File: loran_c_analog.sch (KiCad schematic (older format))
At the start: 54 parts, among them P601 DAC VCO, P602 DAC AGC, P603 LORAN In, P604 RSVD In, Q601 BD135, Q602 BD136, U601 TL072, U602 LD1117S33

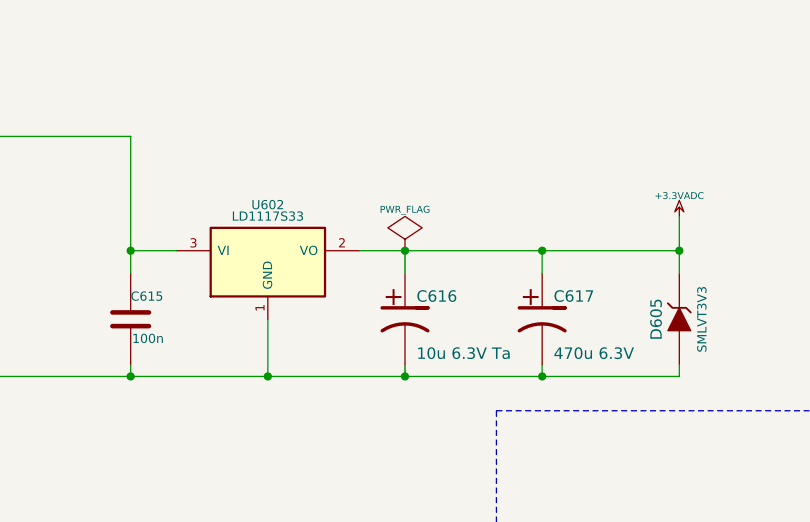
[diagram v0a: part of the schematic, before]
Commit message: FIXED: no more buses on hierarchical sheet ports
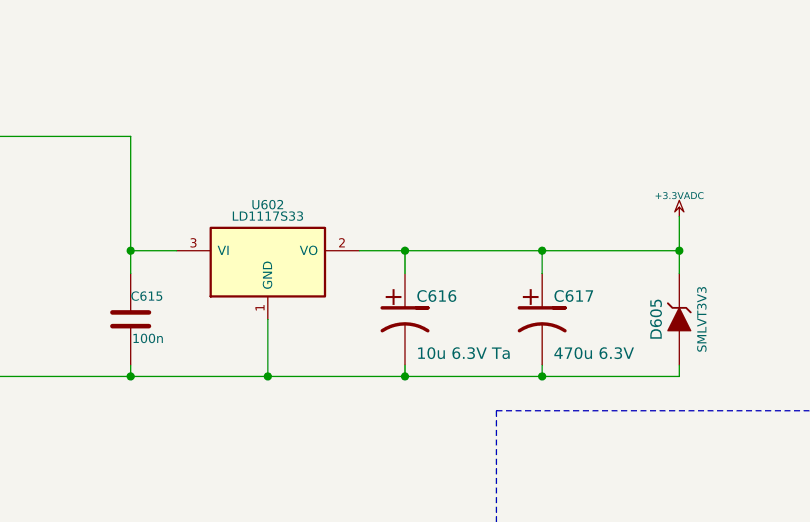
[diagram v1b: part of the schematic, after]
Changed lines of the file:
@@
 $Descr A4 11693 8268
 encoding utf-8
-Sheet 6 7
+Sheet 5 7
 Title "Analog part"
 Date ""
@@
 $EndComp
 $Comp
-L +3.3VADC #PWR088
+L +3.3VADC #PWR081
 U 1 1 52E38762
 P 7700 1650
-F 0 "#PWR088" H 7700 1770 20  0001 C CNN
+F 0 "#PWR081" H 7700 1770 20  0001 C CNN
 F 1 "+3.3VADC" H 7700 1740 30  0000 C CNN
 F 2 "" H 7700 1650 60  0000 C CNN
 F 3 "" H 7700 1650 60  0000 C CNN
 	1    7700 1650
-	1    0    0    -1
-$EndComp
-$Comp
-L PWR_FLAG #FLG089
-U 1 1 52E3A067
-P 6500 1800
-F 0 "#FLG089" H 6500 1895 30  0001 C CNN
-F 1 "PWR_FLAG" H 6500 1980 30  0000 C CNN
-F 2 "" H 6500 1800 60  0000 C CNN
-F 3 "" H 6500 1800 60  0000 C CNN
-	1    6500 1800
 	1    0    0    -1
 $EndComp
@@
 -7.5V
 $Comp
-L AGND #PWR090
+L AGND #PWR082
 U 1 1 52E3C710
 P 1150 2400
-F 0 "#PWR090" H 1150 2400 40  0001 C CNN
+F 0 "#PWR082" H 1150 2400 40  0001 C CNN
 F 1 "AGND" H 1150 2330 50  0000 C CNN
 F 2 "" H 1150 2400 60  0000 C CNN
@@
 $EndComp
 $Comp
-L AGND #PWR091
+L AGND #PWR083
 U 1 1 52E42BA3
 P 3600 4850
-F 0 "#PWR091" H 3600 4850 40  0001 C CNN
+F 0 "#PWR083" H 3600 4850 40  0001 C CNN
 F 1 "AGND" H 3600 4780 50  0000 C CNN
 F 2 "" H 3600 4850 60  0000 C CNN
@@
 $EndComp
 $Comp
-L AGND #PWR092
+L AGND #PWR084
 U 1 1 52E42BAE
 P 3900 4850
-F 0 "#PWR092" H 3900 4850 40  0001 C CNN
+F 0 "#PWR084" H 3900 4850 40  0001 C CNN
 F 1 "AGND" H 3900 4780 50  0000 C CNN
 F 2 "" H 3900 4850 60  0000 C CNN
@@
 $EndComp
 $Comp
-L AGND #PWR093
+L AGND #PWR085
 U 1 1 52E434DA
 P 3600 6550
-F 0 "#PWR093" H 3600 6550 40  0001 C CNN
+F 0 "#PWR085" H 3600 6550 40  0001 C CNN
 F 1 "AGND" H 3600 6480 50  0000 C CNN
 F 2 "" H 3600 6550 60  0000 C CNN
@@
 $EndComp
 $Comp
-L AGND #PWR094
+L AGND #PWR086
 U 1 1 52E434E0
 P 3900 6550
-F 0 "#PWR094" H 3900 6550 40  0001 C CNN
+F 0 "#PWR086" H 3900 6550 40  0001 C CNN
 F 1 "AGND" H 3900 6480 50  0000 C CNN
 F 2 "" H 3900 6550 60  0000 C CNN
@@
 $EndComp
 $Comp
-L PWR_FLAG #FLG095
+L PWR_FLAG #FLG087
 U 1 1 52E43900
 P 4600 1300
-F 0 "#FLG095" H 4600 1395 30  0001 C CNN
+F 0 "#FLG087" H 4600 1395 30  0001 C CNN
 F 1 "PWR_FLAG" H 4600 1480 30  0000 C CNN
 F 2 "" H 4600 1300 60  0000 C CNN
@@
 $EndComp
 $Comp
-L PWR_FLAG #FLG096
+L PWR_FLAG #FLG088
 U 1 1 52E4390B
 P 4600 3400
-F 0 "#FLG096" H 4600 3495 30  0001 C CNN
+F 0 "#FLG088" H 4600 3495 30  0001 C CNN
 F 1 "PWR_FLAG" H 4600 3580 30  0000 C CNN
 F 2 "" H 4600 3400 60  0000 C CNN
@@
 $EndComp
 $Comp
-L AGND #PWR097
+L AGND #PWR089
 U 1 1 52E4434F
 P 4600 5450
-F 0 "#PWR097" H 4600 5450 40  0001 C CNN
+F 0 "#PWR089" H 4600 5450 40  0001 C CNN
 F 1 "AGND" H 4600 5380 50  0000 C CNN
 F 2 "" H 4600 5450 60  0000 C CNN
@@
 $EndComp
 $Comp
-L AGND #PWR098
+L AGND #PWR090
 U 1 1 52E4435A
 P 4600 6550
-F 0 "#PWR098" H 4600 6550 40  0001 C CNN
+F 0 "#PWR090" H 4600 6550 40  0001 C CNN
 F 1 "AGND" H 4600 6480 50  0000 C CNN
 F 2 "" H 4600 6550 60  0000 C CNN
@@
 $EndComp
 $Comp
-L AGND #PWR099
+L AGND #PWR091
 U 1 1 52E476C2
 P 1600 5650
-F 0 "#PWR099" H 1600 5650 40  0001 C CNN
+F 0 "#PWR091" H 1600 5650 40  0001 C CNN
 F 1 "AGND" H 1600 5580 50  0000 C CNN
 F 2 "" H 1600 5650 60  0000 C CNN
@@
 $EndComp
 $Comp
-L AGND #PWR0100
+L AGND #PWR092
 U 1 1 52E4B7B5
 P 7950 4100
-F 0 "#PWR0100" H 7950 4100 40  0001 C CNN
+F 0 "#PWR092" H 7950 4100 40  0001 C CNN
 F 1 "AGND" H 7950 4030 50  0000 C CNN
 F 2 "" H 7950 4100 60  0000 C CNN
@@
 $EndComp
 $Comp
-L AGND #PWR0101
+L AGND #PWR093
 U 1 1 52E4C26B
 P 8450 4100
-F 0 "#PWR0101" H 8450 4100 40  0001 C CNN
+F 0 "#PWR093" H 8450 4100 40  0001 C CNN
 F 1 "AGND" H 8450 4030 50  0000 C CNN
 F 2 "" H 8450 4100 60  0000 C CNN
@@
 $EndComp
 $Comp
-L AGND #PWR0102
+L AGND #PWR094
 U 1 1 52E4D87E
 P 8200 4100
-F 0 "#PWR0102" H 8200 4100 40  0001 C CNN
+F 0 "#PWR094" H 8200 4100 40  0001 C CNN
 F 1 "AGND" H 8200 4030 50  0000 C CNN
 F 2 "" H 8200 4100 60  0000 C CNN
@@
 $EndComp
 $Comp
-L AGND #PWR0103
+L AGND #PWR095
 U 1 1 52E4EBFE
 P 9100 4100
-F 0 "#PWR0103" H 9100 4100 40  0001 C CNN
+F 0 "#PWR095" H 9100 4100 40  0001 C CNN
 F 1 "AGND" H 9100 4030 50  0000 C CNN
 F 2 "" H 9100 4100 60  0000 C CNN
@@
 $EndComp
 $Comp
-L AGND #PWR0104
+L AGND #PWR096
 U 1 1 52E4EC09
 P 9400 4100
-F 0 "#PWR0104" H 9400 4100 40  0001 C CNN
+F 0 "#PWR096" H 9400 4100 40  0001 C CNN
 F 1 "AGND" H 9400 4030 50  0000 C CNN
 F 2 "" H 9400 4100 60  0000 C CNN
@@
 $EndComp
 $Comp
-L +3.3VADC #PWR0105
+L +3.3VADC #PWR097
 U 1 1 52E4EC14
 P 9100 2750
-F 0 "#PWR0105" H 9100 2870 20  0001 C CNN
+F 0 "#PWR097" H 9100 2870 20  0001 C CNN
 F 1 "+3.3VADC" H 9100 2840 30  0000 C CNN
 F 2 "" H 9100 2750 60  0000 C CNN
@@
 $EndComp
 $Comp
-L AGND #PWR0106
+L AGND #PWR098
 U 1 1 52E53548
 P 10250 4100
-F 0 "#PWR0106" H 10250 4100 40  0001 C CNN
+F 0 "#PWR098" H 10250 4100 40  0001 C CNN
 F 1 "AGND" H 10250 4030 50  0000 C CNN
 F 2 "" H 10250 4100 60  0000 C CNN
@@
 $EndComp
 $Comp
-L AGND #PWR0107
+L AGND #PWR099
 U 1 1 52E545C4
 P 7950 5900
-F 0 "#PWR0107" H 7950 5900 40  0001 C CNN
+F 0 "#PWR099" H 7950 5900 40  0001 C CNN
 F 1 "AGND" H 7950 5830 50  0000 C CNN
 F 2 "" H 7950 5900 60  0000 C CNN
@@
 $EndComp
 $Comp
-L AGND #PWR0108
+L AGND #PWR0100
 U 1 1 52E545D0
 P 8450 5900
-F 0 "#PWR0108" H 8450 5900 40  0001 C CNN
+F 0 "#PWR0100" H 8450 5900 40  0001 C CNN
 F 1 "AGND" H 8450 5830 50  0000 C CNN
 F 2 "" H 8450 5900 60  0000 C CNN
@@
 $EndComp
 $Comp
-L AGND #PWR0109
+L AGND #PWR0101
 U 1 1 52E545EF
 P 8200 5900
-F 0 "#PWR0109" H 8200 5900 40  0001 C CNN
+F 0 "#PWR0101" H 8200 5900 40  0001 C CNN
 F 1 "AGND" H 8200 5830 50  0000 C CNN
 F 2 "" H 8200 5900 60  0000 C CNN
@@
 $EndComp
 $Comp
-L AGND #PWR0110
+L AGND #PWR0102
 U 1 1 52E54601
 P 9100 5900
-F 0 "#PWR0110" H 9100 5900 40  0001 C CNN
+F 0 "#PWR0102" H 9100 5900 40  0001 C CNN
 F 1 "AGND" H 9100 5830 50  0000 C CNN
 F 2 "" H 9100 5900 60  0000 C CNN
@@
 $EndComp
 $Comp
-L AGND #PWR0111
+L AGND #PWR0103
 U 1 1 52E54607
 P 9400 5900
-F 0 "#PWR0111" H 9400 5900 40  0001 C CNN
+F 0 "#PWR0103" H 9400 5900 40  0001 C CNN
 F 1 "AGND" H 9400 5830 50  0000 C CNN
 F 2 "" H 9400 5900 60  0000 C CNN
@@
 $EndComp
 $Comp
-L +3.3VADC #PWR0112
+L +3.3VADC #PWR0104
 U 1 1 52E5460D
 P 9100 4550
-F 0 "#PWR0112" H 9100 4670 20  0001 C CNN
+F 0 "#PWR0104" H 9100 4670 20  0001 C CNN
 F 1 "+3.3VADC" H 9100 4640 30  0000 C CNN
 F 2 "" H 9100 4550 60  0000 C CNN
@@
 $EndComp
 $Comp
-L AGND #PWR0113
+L AGND #PWR0105
 U 1 1 52E54639
 P 10250 5900
-F 0 "#PWR0113" H 10250 5900 40  0001 C CNN
+F 0 "#PWR0105" H 10250 5900 40  0001 C CNN
 F 1 "AGND" H 10250 5830 50  0000 C CNN
 F 2 "" H 10250 5900 60  0000 C CNN
@@
 Connection ~ 5900 2350
 Wire Wire Line
-	6500 1900 6500 1800
-Wire Wire Line
 	6300 1800 7700 1800
 Wire Wire Line
@@
 	7100 2300 7100 2350
 Connection ~ 7100 2350
+Wire Wire Line
+	6500 1800 6500 1900
 $EndSCHEMATC

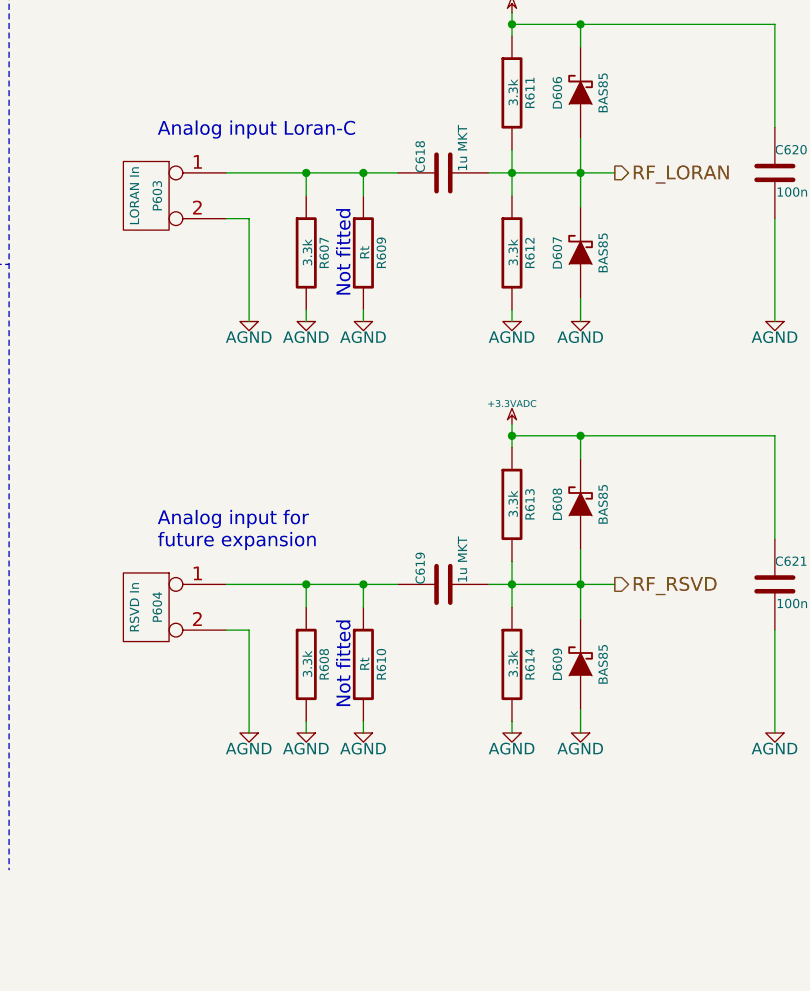
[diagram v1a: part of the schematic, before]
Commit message: Update: fix, assign modules to components -Fix P302 incorrect connection -Assign footprints to components (not all yet) -Back-import footprints into schematic fields
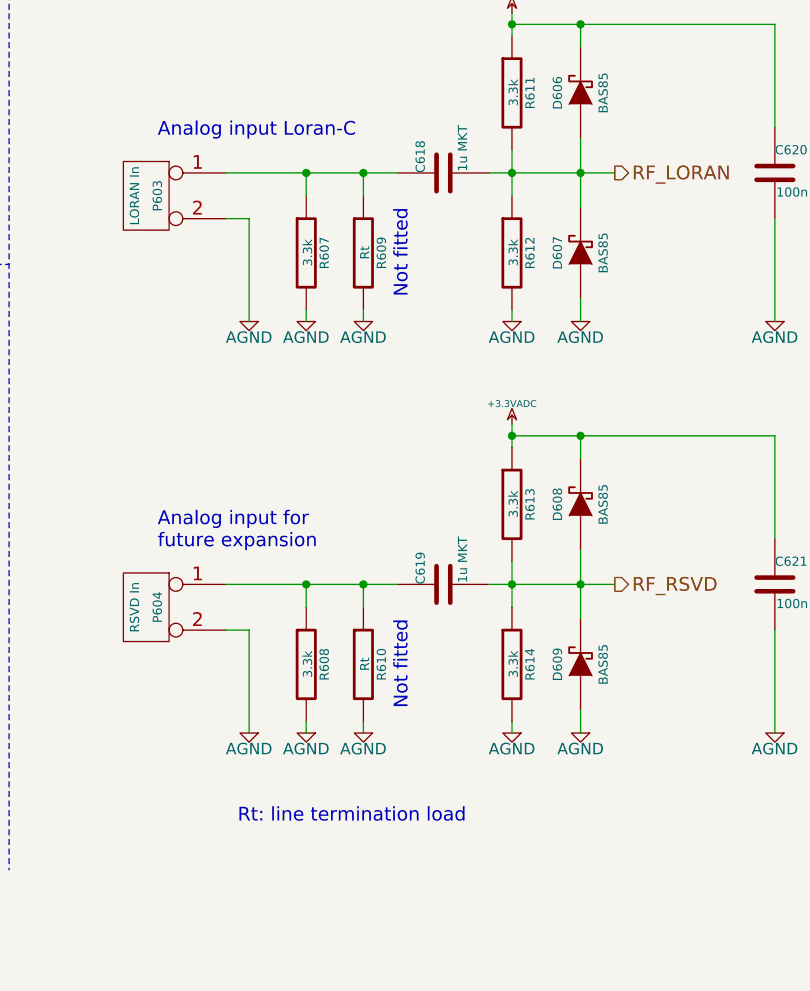
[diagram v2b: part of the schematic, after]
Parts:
- C601, C602, C603, C604, C609, C610, C615, C620, C621: footprint (none) -> w_smd_capacitors:c_1206
- C605, C606, C617: footprint (none) -> w_pth_capacitors:CP_6.3x11mm
- C607, C608: footprint (none) -> w_pth_capacitors:CP_5x11mm
- C611, C612, C616: footprint (none) -> w_smd_capacitors:c_tant_B
- C613, C614: footprint (none) -> w_pth_capacitors:CP_10x12.5mm
- C618, C619: footprint (none) -> w_pth_capacitors:cnp_7x6mm
- D601, D602: footprint (none) -> w_pth_diodes:diode_do41
- D603, D604: footprint (none) -> w_pth_diodes:diode_do15
- D605: footprint (none) -> w_smd_diode:do214aa
- D606, D607, D608, D609: footprint (none) -> w_smd_diode:sod80c
- FB601, FB602, R603, R604, R609, R610: footprint (none) -> w_pth_resistors:RC07
- P601, P602, P603, P604: footprint (none) -> w_conn_kk100:kk100_22-23-2021
- Q601, Q602: footprint TO126 -> Housings_SOT:SOT126_SOT32_Housing_Horizontal_RevA_22Oct2012
- R601, R602, R605, R606, R607, R608, R611, R612, R613, R614: footprint (none) -> w_smd_resistors:r_1206
- U601: footprint (none) -> w_pth_ic:dil_8-300
- U602: footprint (none) -> SMD_Packages:SOT223
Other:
- note added: "Rt: line termination load"
